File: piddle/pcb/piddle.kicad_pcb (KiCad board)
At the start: 2 copper layers, 118 x 104.8 mm, 32 parts, among them J1 Conn_01x03_Socket, J10 Conn_01x03_Socket, J2 Conn_01x03_Socket, J3 Conn_01x03_Socket, J4 Conn_01x03_Socket, J5 Conn_01x03_Socket, J6 Conn_01x03_Socket, J7 Conn_01x03_Socket, J8 Conn_01x03_Socket, J9 Conn_01x03_Socket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

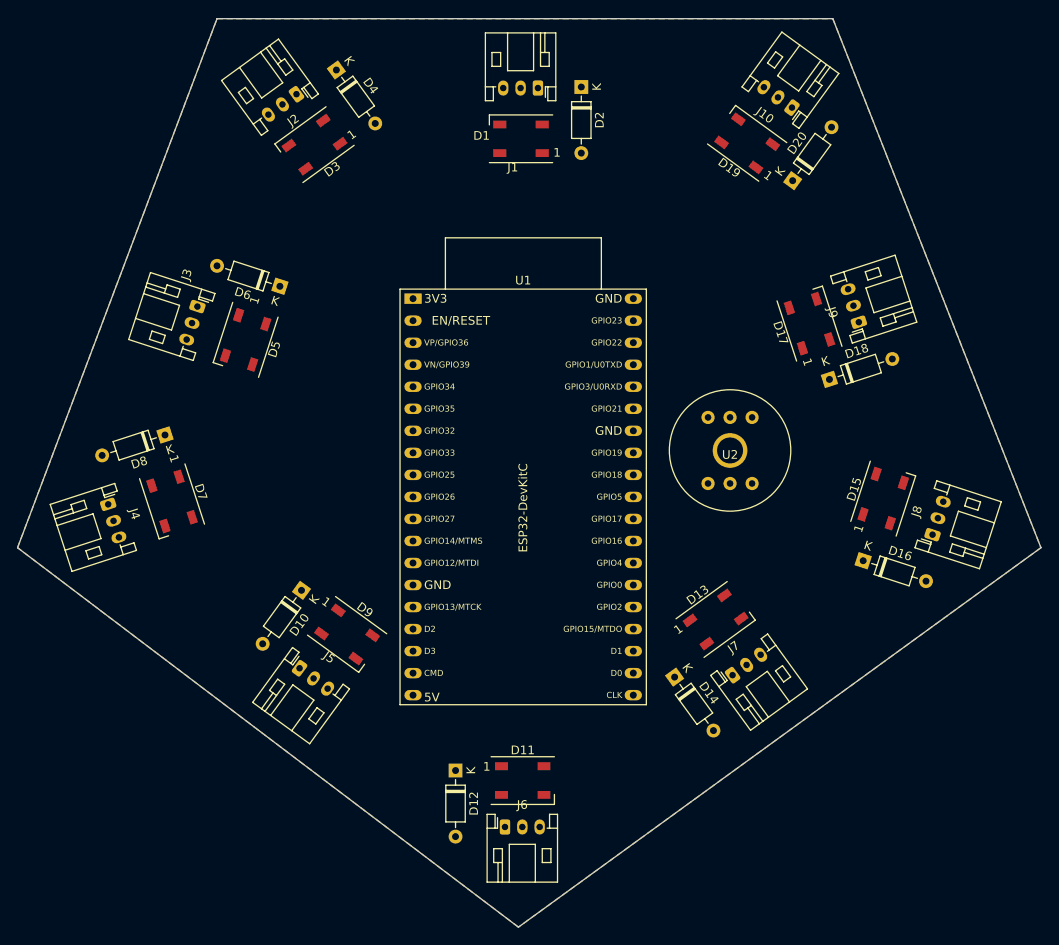
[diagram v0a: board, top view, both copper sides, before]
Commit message: Less tangled GPIO
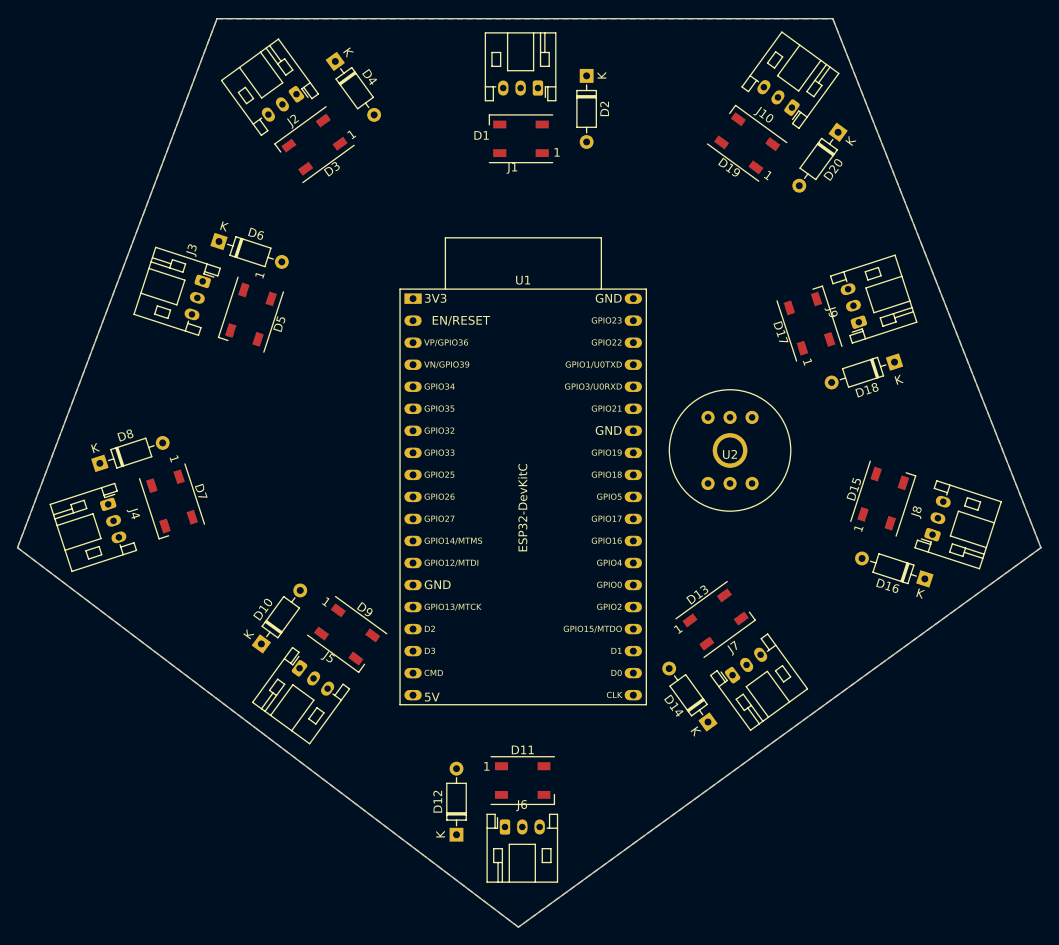
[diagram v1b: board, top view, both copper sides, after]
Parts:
- moved D6 8.71 mm to (70.2, 85.7), turned to -18 degrees
- moved D8 8.19 mm to (56.5, 111.3), turned to 18 degrees
- moved D18 7.76 mm to (148.1, 99.6), turned to -162 degrees
- moved D10 7.72 mm to (75.1, 132.1), turned to 54 degrees
- moved D20 7.66 mm to (141.6, 73.1), turned to -126 degrees
- moved D16 7.42 mm to (151.6, 124.6), turned to 162 degrees
- moved D12 7.41 mm to (97.6, 154.1), turned to 90 degrees
- moved D14 6.45 mm to (126.6, 141.1), turned to 126 degrees
- moved D5 2.97 mm to (73.9, 94.1)
- moved J3 2.97 mm to (68.3, 90.3)
- moved D2 1.42 mm to (112.6, 66.6)
- moved D4 0.99 mm to (83.6, 64.9)
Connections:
- D17 pad 4: /GPIO5 -> /GPIO21
- D19 pad 4: /GPIO18 -> /GPIO22
- U2 pad 3: /GPIO21 -> /GPIO19
- U2 pad 5: /GPIO22 -> /GPIO18
- U2 pad 6: /GPIO19 -> /GPIO5

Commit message: Add resistors for each data line
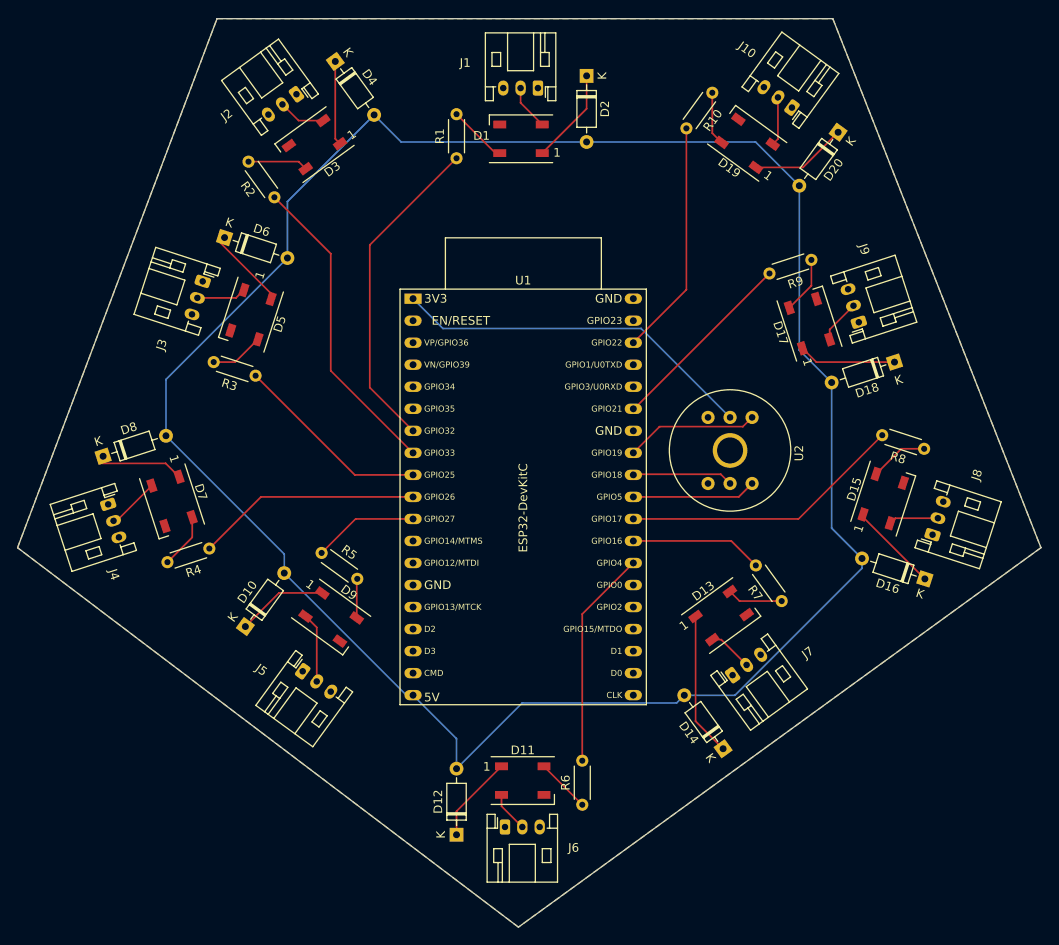
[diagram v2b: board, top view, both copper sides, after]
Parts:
- added R1: R, Resistor_THT:R_Axial_DIN0204_L3.6mm_D1.6mm_P5.08mm_Horizontal, F.Cu at (97.6, 76.1)
- added R10: R, Resistor_THT:R_Axial_DIN0204_L3.6mm_D1.6mm_P5.08mm_Horizontal, F.Cu at (127.1, 68.5)
- added R2: R, Resistor_THT:R_Axial_DIN0204_L3.6mm_D1.6mm_P5.08mm_Horizontal, F.Cu at (76.6, 80.6)
- added R3: R, Resistor_THT:R_Axial_DIN0204_L3.6mm_D1.6mm_P5.08mm_Horizontal, F.Cu at (74.4, 101.2)
- added R4: R, Resistor_THT:R_Axial_DIN0204_L3.6mm_D1.6mm_P5.08mm_Horizontal, F.Cu at (69.1, 121.1)
- added R5: R, Resistor_THT:R_Axial_DIN0204_L3.6mm_D1.6mm_P5.08mm_Horizontal, F.Cu at (82.1, 121.6)
- added R6: R, Resistor_THT:R_Axial_DIN0204_L3.6mm_D1.6mm_P5.08mm_Horizontal, F.Cu at (112.1, 150.6)
- added R7: R, Resistor_THT:R_Axial_DIN0204_L3.6mm_D1.6mm_P5.08mm_Horizontal, F.Cu at (135.1, 127.2)
- added R8: R, Resistor_THT:R_Axial_DIN0204_L3.6mm_D1.6mm_P5.08mm_Horizontal, F.Cu at (151.5, 109.6)
- added R9: R, Resistor_THT:R_Axial_DIN0204_L3.6mm_D1.6mm_P5.08mm_Horizontal, F.Cu at (138.5, 87.8)
- moved D14 3.54 mm to (128.4, 144.2)
- moved D10 2.73 mm to (73.3, 130.1)
- moved D9 2.73 mm to (83.2, 129.0)
- moved D8 0.90 mm to (56.9, 110.5)
- moved D6 0.78 mm to (70.9, 85.2)
- moved D13 0.78 mm to (128.1, 128.8)
- moved J5 0.50 mm to (79.9, 135.2)
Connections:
- D1 pad 4: /GPIO32 -> Net-(D1-DIN)
- D11 pad 4: /GPIO4 -> Net-(D11-DIN)
- D13 pad 4: /GPIO16 -> Net-(D13-DIN)
- D15 pad 4: /GPIO17 -> Net-(D15-DIN)
- D17 pad 4: /GPIO21 -> Net-(D17-DIN)
- D19 pad 4: /GPIO22 -> Net-(D19-DIN)
- D3 pad 4: /GPIO33 -> Net-(D3-DIN)
- D5 pad 4: /GPIO25 -> Net-(D5-DIN)
- D7 pad 4: /GPIO26 -> Net-(D7-DIN)
- D9 pad 4: /GPIO27 -> Net-(D9-DIN)
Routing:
- net /5V: track 0.00 -> 255.5 mm
- net /3V3: track 0.00 -> 42.2 mm
- net /GPIO32: track 0.00 -> 37.6 mm
- net /GPIO33: track 0.00 -> 36.1 mm
- net /GPIO17: track 0.00 -> 32.7 mm
- net /GPIO22: track 0.00 -> 27.2 mm
- net /GPIO26: track 0.00 -> 26.0 mm
- net /GPIO4: track 0.00 -> 25.2 mm
- net /GPIO25: track 0.00 -> 22.9 mm
- net /GPIO21: track 0.00 -> 22.2 mm
- net Net-(D13-VDD): track 0.00 -> 16.6 mm
- net /GPIO19: track 0.00 -> 15.4 mm
- net /GPIO16: track 0.00 -> 15.3 mm
- net /GPIO5: track 0.00 -> 14.3 mm
- net /GPIO27: track 0.00 -> 12.2 mm
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
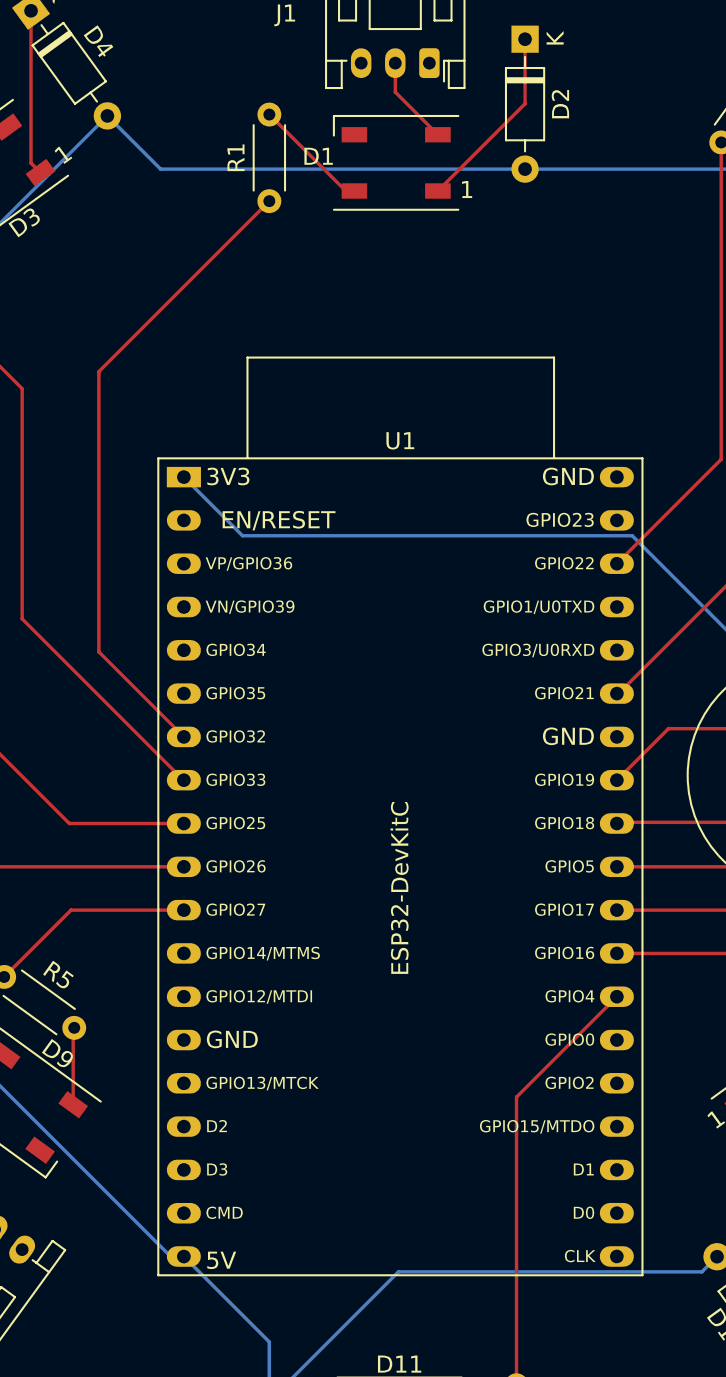
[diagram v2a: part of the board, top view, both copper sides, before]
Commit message: Add ground plane on back copper
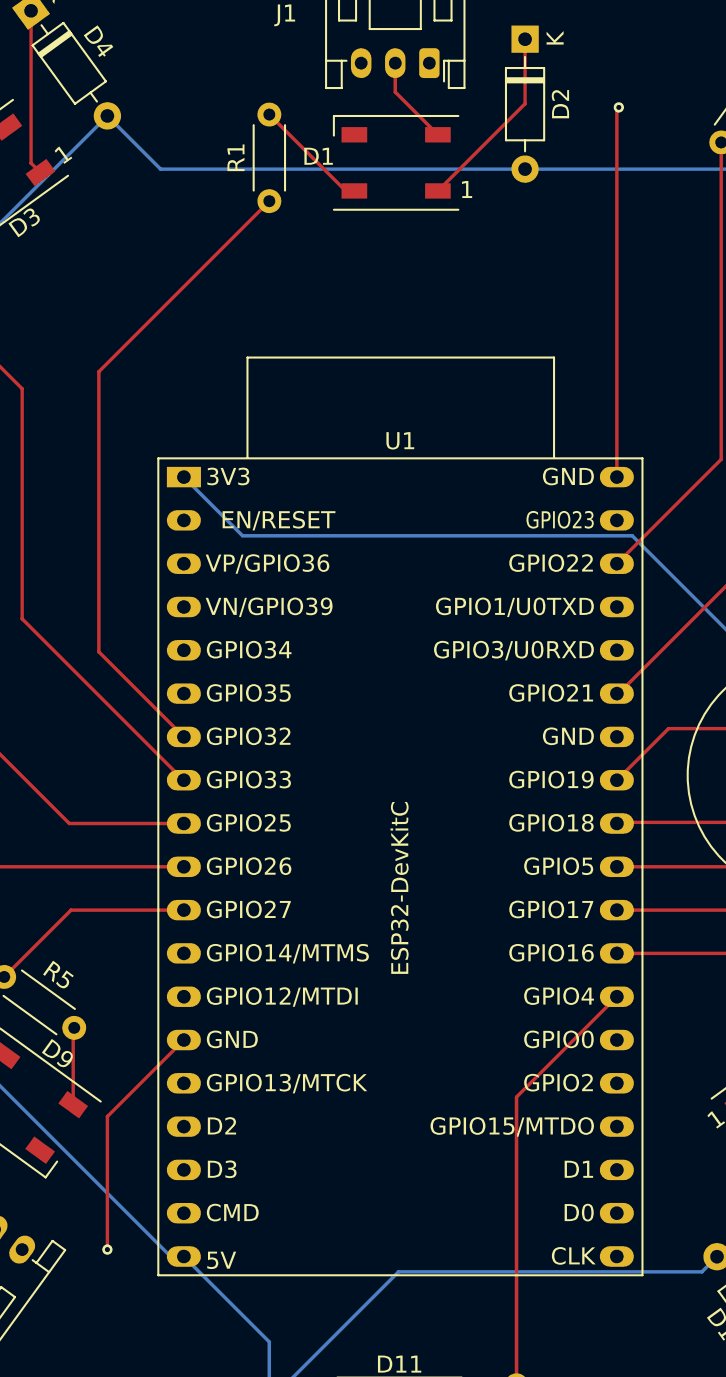
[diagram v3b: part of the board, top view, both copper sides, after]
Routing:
- net /GND: track 0.00 -> 35.9 mm, vias 0 -> 2
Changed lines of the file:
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@@
     )
     (fp_text user "GPIO35" (at 1.27 12.7 unlocked) (layer "F.SilkS")
-        (effects (font (size 0.7 0.7) (thickness 0.15)) (justify left))
+        (effects (font (size 1 1) (thickness 0.15)) (justify left))
     )
     (fp_text user "GPIO5" (at 24.13 22.86 unlocked) (layer "F.SilkS")
-        (effects (font (size 0.7 0.7) (thickness 0.15)) (justify right))
+        (effects (font (size 1 1) (thickness 0.15)) (justify right))
     )
     (fp_text user "GPIO13/MTCK" (at 1.27 35.56 unlocked) (layer "F.SilkS")
-        (effects (font (size 0.7 0.7) (thickness 0.15)) (justify left))
+        (effects (font (size 1 1) (thickness 0.15)) (justify left))
     )
     (fp_text user "GPIO33" (at 1.27 17.78 unlocked) (layer "F.SilkS")
-        (effects (font (size 0.7 0.7) (thickness 0.15)) (justify left))
+        (effects (font (size 1 1) (thickness 0.15)) (justify left))
     )
     (fp_text user "GPIO15/MTDO" (at 24.13 38.1 unlocked) (layer "F.SilkS")
-        (effects (font (size 0.7 0.7) (thickness 0.15)) (justify right))
+        (effects (font (size 1 1) (thickness 0.15)) (justify right))
     )
     (fp_text user "VP/GPIO36" (at 1.27 5.08 unlocked) (layer "F.SilkS")
-        (effects (font (size 0.7 0.7) (thickness 0.15)) (justify left))
+        (effects (font (size 1 1) (thickness 0.15)) (justify left))
     )
     (fp_text user "GPIO4" (at 24.13 30.48 unlocked) (layer "F.SilkS")
-        (effects (font (size 0.7 0.7) (thickness 0.15)) (justify right))
+        (effects (font (size 1 1) (thickness 0.15)) (justify right))
     )
     (fp_text user "GPIO0" (at 24.13 33.02 unlocked) (layer "F.SilkS")
-        (effects (font (size 0.7 0.7) (thickness 0.15)) (justify right))
+        (effects (font (size 1 1) (thickness 0.15)) (justify right))
     )
     (fp_text user "EN/RESET" (at 8.88632 2.53728 unlocked) (layer "F.SilkS")
@@
     )
     (fp_text user "GPIO3/U0RXD" (at 24.13 10.16 unlocked) (layer "F.SilkS")
-        (effects (font (size 0.7 0.7) (thickness 0.15)) (justify right))
+        (effects (font (size 1 1) (thickness 0.15)) (justify right))
     )
     (fp_text user "GPIO26" (at 1.27 22.86 unlocked) (layer "F.SilkS")
-        (effects (font (size 0.7 0.7) (thickness 0.15)) (justify left))
+        (effects (font (size 1 1) (thickness 0.15)) (justify left))
     )
     (fp_text user "GND" (at 24.13 15.24 unlocked) (layer "F.SilkS")
@@
     )
     (fp_text user "GPIO14/MTMS" (at 1.27 27.94 unlocked) (layer "F.SilkS")
-        (effects (font (size 0.7 0.7) (thickness 0.15)) (justify left))
+        (effects (font (size 1 1) (thickness 0.15)) (justify left))
     )
     (fp_text user "D1" (at 24.13 40.64 unlocked) (layer "F.SilkS")
-        (effects (font (size 0.7 0.7) (thickness 0.15)) (justify right))
+        (effects (font (size 1 1) (thickness 0.15)) (justify right))
     )
     (fp_text user "CMD" (at 1.27 43.18 unlocked) (layer "F.SilkS")
-        (effects (font (size 0.7 0.7) (thickness 0.15)) (justify left))
+        (effects (font (size 1 1) (thickness 0.15)) (justify left))
     )
     (fp_text user "VN/GPIO39" (at 1.27 7.62 unlocked) (layer "F.SilkS")
-        (effects (font (size 0.7 0.7) (thickness 0.15)) (justify left))
+        (effects (font (size 1 1) (thickness 0.15)) (justify left))
     )
     (fp_text user "GPIO22" (at 24.13 5.08 unlocked) (layer "F.SilkS")
-        (effects (font (size 0.7 0.7) (thickness 0.15)) (justify right))
+        (effects (font (size 1 1) (thickness 0.15)) (justify right))
     )
     (fp_text user "GPIO27" (at 1.27 25.4 unlocked) (layer "F.SilkS")
-        (effects (font (size 0.7 0.7) (thickness 0.15)) (justify left))
+        (effects (font (size 1 1) (thickness 0.15)) (justify left))
     )
     (fp_text user "GPIO21" (at 24.13 12.7 unlocked) (layer "F.SilkS")
-        (effects (font (size 0.7 0.7) (thickness 0.15)) (justify right))
+        (effects (font (size 1 1) (thickness 0.15)) (justify right))
     )
     (fp_text user "GPIO34" (at 1.27 10.16 unlocked) (layer "F.SilkS")
-        (effects (font (size 0.7 0.7) (thickness 0.15)) (justify left))
+        (effects (font (size 1 1) (thickness 0.15)) (justify left))
     )
     (fp_text user "GPIO18" (at 24.13 20.32 unlocked) (layer "F.SilkS")
-        (effects (font (size 0.7 0.7) (thickness 0.15)) (justify right))
+        (effects (font (size 1 1) (thickness 0.15)) (justify right))
     )
     (fp_text user "GPIO2" (at 24.13 35.56 unlocked) (layer "F.SilkS")
-        (effects (font (size 0.7 0.7) (thickness 0.15)) (justify right))
+        (effects (font (size 1 1) (thickness 0.15)) (justify right))
     )
     (fp_text user "GPIO19" (at 24.13 17.78 unlocked) (layer "F.SilkS")
-        (effects (font (size 0.7 0.7) (thickness 0.15)) (justify right))
+        (effects (font (size 1 1) (thickness 0.15)) (justify right))
     )
     (fp_text user "D0" (at 24.13 43.18 unlocked) (layer "F.SilkS")
-        (effects (font (size 0.7 0.7) (thickness 0.15)) (justify right))
+        (effects (font (size 1 1) (thickness 0.15)) (justify right))
     )
     (fp_text user "D2" (at 1.27 38.1 unlocked) (layer "F.SilkS")
-        (effects (font (size 0.7 0.7) (thickness 0.15)) (justify left))
+        (effects (font (size 1 1) (thickness 0.15)) (justify left))
     )
     (fp_text user "D3" (at 1.27 40.64 unlocked) (layer "F.SilkS")
-        (effects (font (size 0.7 0.7) (thickness 0.15)) (justify left))
+        (effects (font (size 1 1) (thickness 0.15)) (justify left))
     )
     (fp_text user "GPIO17" (at 24.13 25.4 unlocked) (layer "F.SilkS")
-        (effects (font (size 0.7 0.7) (thickness 0.15)) (justify right))
+        (effects (font (size 1 1) (thickness 0.15)) (justify right))
     )
     (fp_text user "GPIO1/U0TXD" (at 24.13 7.62 unlocked) (layer "F.SilkS")
-        (effects (font (size 0.7 0.7) (thickness 0.15)) (justify right))
+        (effects (font (size 1 1) (thickness 0.15)) (justify right))
     )
     (fp_text user "GPIO32" (at 1.27 15.24 unlocked) (layer "F.SilkS")
-        (effects (font (size 0.7 0.7) (thickness 0.15)) (justify left))
+        (effects (font (size 1 1) (thickness 0.15)) (justify left))
     )
     (fp_text user "GPIO16" (at 24.13 27.94 unlocked) (layer "F.SilkS")
-        (effects (font (size 0.7 0.7) (thickness 0.15)) (justify right))
+        (effects (font (size 1 1) (thickness 0.15)) (justify right))
     )
     (fp_text user "3V3" (at 1.27 0 unlocked) (layer "F.SilkS")
@@
     )
     (fp_text user "CLK" (at 24.13 45.72 unlocked) (layer "F.SilkS")
-        (effects (font (size 0.7 0.7) (thickness 0.15)) (justify right))
+        (effects (font (size 1 1) (thickness 0.15)) (justify right))
     )
     (fp_text user "GPIO25" (at 1.27 20.32 unlocked) (layer "F.SilkS")
-        (effects (font (size 0.7 0.7) (thickness 0.15)) (justify left))
+        (effects (font (size 1 1) (thickness 0.15)) (justify left))
     )
     (fp_text user "GPIO12/MTDI" (at 1.27 30.48 unlocked) (layer "F.SilkS")
-        (effects (font (size 0.7 0.7) (thickness 0.15)) (justify left))
+        (effects (font (size 1 1) (thickness 0.15)) (justify left))
     )
     (fp_text user "GPIO23" (at 24.13 2.54 unlocked) (layer "F.SilkS")
-        (effects (font (size 0.8 0.8) (thickness 0.15)) (justify right))
+        (effects (font (size 1 0.8) (thickness 0.15)) (justify right))
     )
     (fp_text user "GND" (at 1.27 33.02 unlocked) (layer "F.SilkS")
@@
   (segment (start 85.979026 117.68272) (end 82.058377 121.603369) (width 0.2) (layer "F.Cu") (net 9))
   (segment (start 92.6 117.68272) (end 85.979026 117.68272) (width 0.2) (layer "F.Cu") (net 9))
+  (segment (start 118 70.709623) (end 118.11328 70.596343) (width 0.2) (layer "F.Cu") (net 12))
+  (segment (start 88.11328 129.78944) (end 88.11328 137.596343) (width 0.2) (layer "F.Cu") (net 12))
+  (segment (start 92.6 125.30272) (end 88.11328 129.78944) (width 0.2) (layer "F.Cu") (net 12))
+  (segment (start 118 92.28272) (end 118 70.709623) (width 0.2) (layer "F.Cu") (net 12))
+  (via (at 118.11328 70.596343) (size 0.6) (drill 0.3) (layers "F.Cu" "B.Cu") (net 12))
+  (via (at 88.11328 137.596343) (size 0.6) (drill 0.3) (layers "F.Cu" "B.Cu") (net 12))
   (segment (start 112.11328 145.556343) (end 112.11328 128.64944) (width 0.2) (layer "F.Cu") (net 23))
   (segment (start 112.11328 128.64944) (end 118 122.76272) (width 0.2) (layer "F.Cu") (net 23))
